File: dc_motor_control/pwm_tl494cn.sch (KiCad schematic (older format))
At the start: 31 parts

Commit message: New PCB for DC motor control
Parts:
- removed U?: L7812, symbol L7812
- added C1: 2200uF, Capacitors_ThroughHole:CP_Radial_D12.5mm_P5.00mm, symbol CP
- added C6: 1uF, Capacitors_ThroughHole:C_Rect_L4.6mm_W2.0mm_P2.50mm_MKS02_FKP02, symbol C
- added C7: 100nF, Capacitors_ThroughHole:C_Rect_L4.6mm_W2.0mm_P2.50mm_MKS02_FKP02, symbol C
- added D1: 15V, Diodes_ThroughHole:D_T-1_P5.08mm_Horizontal, symbol D_Zener
- added D6: LED, LEDs:LED_D4.0mm, symbol LED
- added J2: 12V_SEL, Pin_Headers:Pin_Header_Straight_1x03_Pitch2.54mm, symbol Conn_01x03
- added Q1: RFP70N06, TO_SOT_Packages_THT:TO-220-3_Vertical, symbol IRF540N
- added R1: 10R, Capacitors_ThroughHole:C_Rect_L4.6mm_W2.0mm_P2.50mm_MKS02_FKP02, symbol R
- added R13: 330R, Capacitors_ThroughHole:C_Rect_L4.6mm_W2.0mm_P2.50mm_MKS02_FKP02, symbol R
- added R14: 2K7, Capacitors_ThroughHole:C_Rect_L4.6mm_W2.0mm_P2.50mm_MKS02_FKP02, symbol R
- added R6: 1K, Capacitors_ThroughHole:C_Rect_L4.6mm_W2.0mm_P2.50mm_MKS02_FKP02, symbol R
- added U1: LM317, TO_SOT_Packages_SMD:SOT-223-3_TabPin2, symbol LM317_3PinPackage
- C2: renamed from C?; value 100uF -> 10uF; footprint (none) -> Capacitors_ThroughHole:CP_Radial_D4.0mm_P2.00mm
- C3, C4, C5: renamed from C?; footprint Capacitors_ThroughHole:C_Rect_L4_W2.5_P2.5 -> Capacitors_ThroughHole:C_Rect_L4.6mm_W2.0mm_P2.50mm_MKS02_FKP02
- D2, D3, D4, D5: renamed from D?; footprint (none) -> Diodes_ThroughHole:D_T-1_P5.08mm_Horizontal
- D7, D8: renamed from D?; footprint (none) -> TO_SOT_Packages_THT:TO-220-2_Vertical
- F1: renamed from F?; footprint (none) -> Fuse_Holders_and_Fuses:Fuse_SMD1206_Wave
- J1, J3: renamed from J?; footprint (none) -> Terminal_Blocks:TerminalBlock_Altech_AK300-2_P5.00mm
- Q2, Q3, Q4: renamed from Q?; footprint TO_SOT_Packages_THT:TO-220_Vertical -> TO_SOT_Packages_THT:TO-220-3_Vertical
- R10, R11, R12, R2, R3, R4, R5, R7, R8, R9: renamed from R?; footprint Resistors_Universal:Resistor_SMD+THTuniversal_2512_RM10_HandSoldering -> Capacitors_ThroughHole:C_Rect_L4.6mm_W2.0mm_P2.50mm_MKS02_FKP02
- RV1: renamed from RV?; value POT -> 5K; footprint (none) -> Potentiometers:Potentiometer_Piher_T16H_Single_Vertical
- U2: renamed from U?; footprint (none) -> SMD_Packages:SO-16-N
- gave numbers to parts that had none: 2
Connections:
- net +12V: now also R6.2
- net GND: now also RV1.3, C1.2, C6.2, C7.2, D1.2 (A), D6.1 (K), Q1.3 (S), R14.2; no longer RV1.1
- net at C5.2, R12.1, U2.14 (Vref): now also RV1.1; no longer RV1.3
- net at R5.2: now also J2.2 (Pin_2)
- net at D7.1 (K), D8.1 (K), F1.2: now also J3.1 (Pin_1), C1.1, C7.1, J2.3 (Pin_3), U1.3 (VI); no longer J3.2 (Pin_2)
- net at D7.2 (A), D8.2 (A), Q2.2 (D)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: now also J3.2 (Pin_2), Q1.2 (D); no longer J3.1 (Pin_1)
- net at D5.2 (A), R2.1, R3.1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: now also R1.1
- new net: D6.2 (A), R6.1
- new net: C6.1, J2.1 (Pin_1), R13.1, U1.2 (VO)
- new net: D1.1 (K), Q1.1 (G), R1.2
- new net: R13.2, R14.1, U1.1 (ADJ)
- no-connect marks 0 -> 1
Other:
- moved on the sheet: C2, C3, C4, C5, D2, D3, D4, D5, D7, D8, F1, J1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

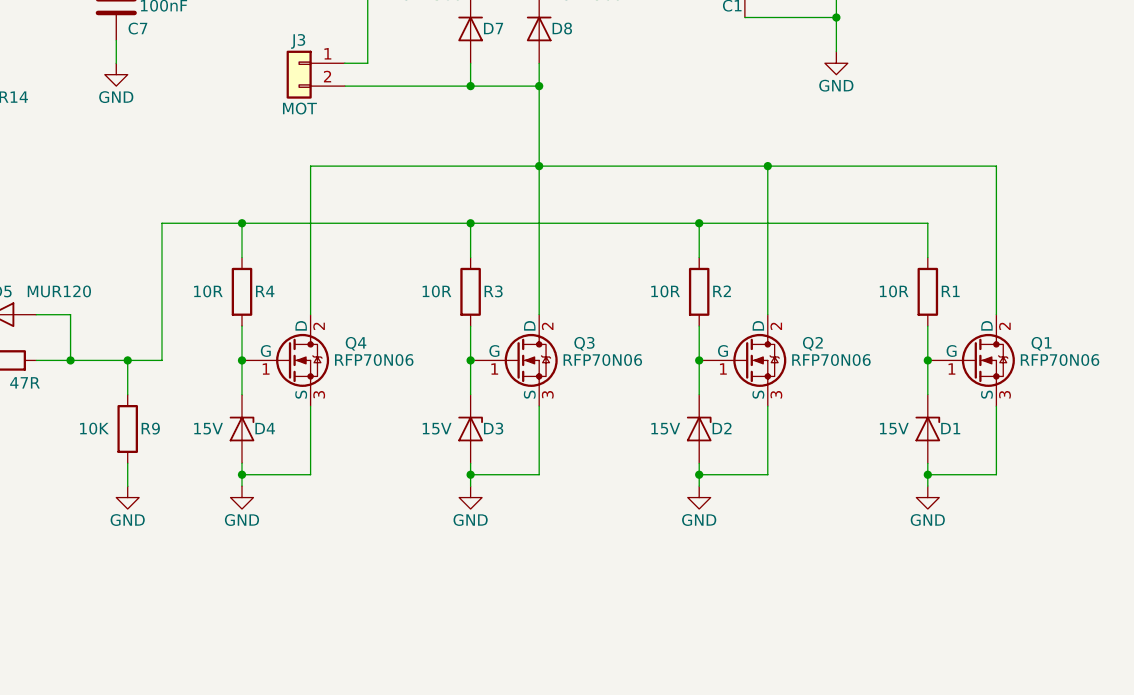
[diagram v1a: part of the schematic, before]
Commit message: Refining the DC motor control some more
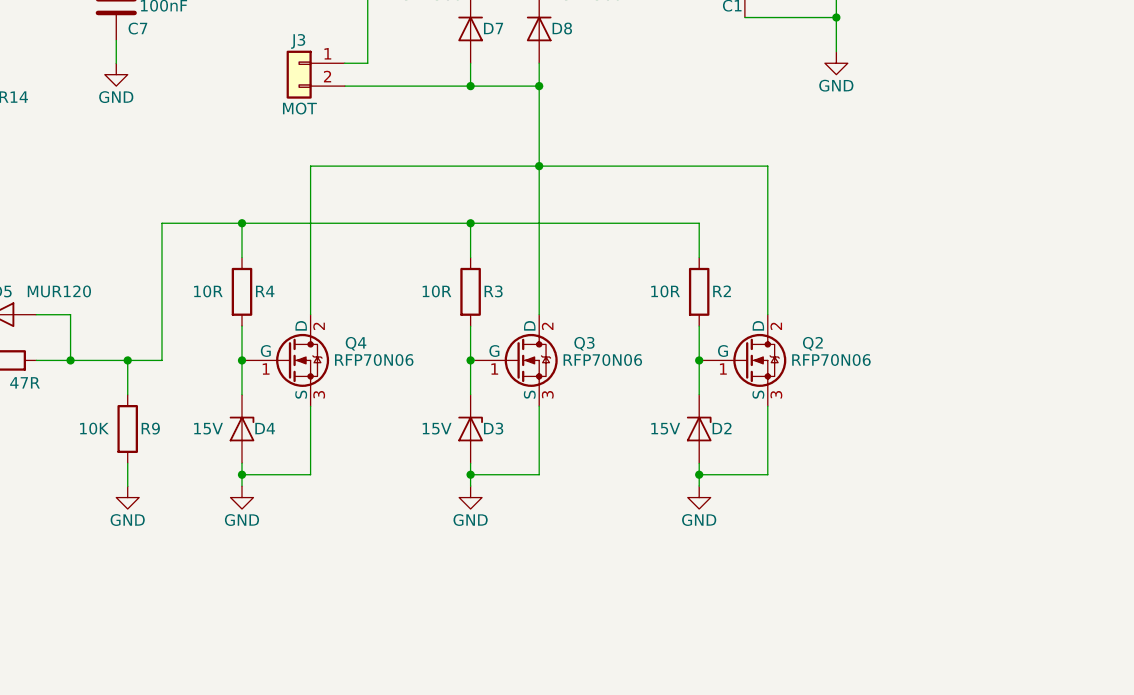
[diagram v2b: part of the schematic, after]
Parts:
- removed D1: 15V, Diodes_ThroughHole:D_T-1_P5.08mm_Horizontal, symbol D_Zener
- removed Q1: RFP70N06, TO_SOT_Packages_THT:TO-220-3_Vertical, symbol IRF540N
- removed R1: 10R, Capacitors_ThroughHole:C_Rect_L4.6mm_W2.0mm_P2.50mm_MKS02_FKP02, symbol R
- J1, J3: footprint Terminal_Blocks:TerminalBlock_Altech_AK300-2_P5.00mm -> Terminal_Blocks:TerminalBlock_bornier-2_P5.08mm
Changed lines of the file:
@@
 F 0 "J1" H 9900 2550 50  0000 C CNN
 F 1 "PWR" H 9900 2250 50  0000 C CNN
-F 2 "Terminal_Blocks:TerminalBlock_Altech_AK300-2_P5.00mm" H 9900 2450 50  0001 C CNN
+F 2 "Terminal_Blocks:TerminalBlock_bornier-2_P5.08mm" H 9900 2450 50  0001 C CNN
 F 3 "" H 9900 2450 50  0001 C CNN
 	1    9900 2450
@@
 F 0 "J3" H 6800 3050 50  0000 C CNN
 F 1 "MOT" H 6800 2750 50  0000 C CNN
-F 2 "Terminal_Blocks:TerminalBlock_Altech_AK300-2_P5.00mm" H 6800 2950 50  0001 C CNN
+F 2 "Terminal_Blocks:TerminalBlock_bornier-2_P5.08mm" H 6800 2950 50  0001 C CNN
 F 3 "" H 6800 2950 50  0001 C CNN
 	1    6800 2950
@@
 $EndComp
 $Comp
-L IRF540N Q1
-U 1 1 5B9B1991
-P 9750 4250
-F 0 "Q1" H 10000 4325 50  0000 L CNN
-F 1 "RFP70N06" H 9950 4250 50  0000 L CNN
-F 2 "TO_SOT_Packages_THT:TO-220-3_Vertical" H 10000 4175 50  0001 L CIN
-F 3 "" H 9750 4250 50  0001 L CNN
-	1    9750 4250
-	1    0    0    -1
-$EndComp
-$Comp
-L R R1
-U 1 1 5B9B1A3F
-P 9550 3950
-F 0 "R1" H 9650 3950 50  0000 C CNN
-F 1 "10R" H 9400 3950 50  0000 C CNN
-F 2 "Capacitors_ThroughHole:C_Rect_L4.6mm_W2.0mm_P2.50mm_MKS02_FKP02" V 9480 3950 50  0001 C CNN
-F 3 "" H 9550 3950 50  0000 C CNN
-	1    9550 3950
-	1    0    0    -1
-$EndComp
-$Comp
-L D_Zener D1
-U 1 1 5B9B1AE4
-P 9550 4550
-F 0 "D1" V 9550 4650 50  0000 C CNN
-F 1 "15V" V 9550 4400 50  0000 C CNN
-F 2 "Diodes_ThroughHole:D_T-1_P5.08mm_Horizontal" H 9550 4550 50  0001 C CNN
-F 3 "" H 9550 4550 50  0001 C CNN
-	1    9550 4550
-	0    1    1    0
-$EndComp
-$Comp
-L GND #PWR015
-U 1 1 5B9B1B8A
-P 9550 4800
-F 0 "#PWR015" H 9550 4550 50  0001 C CNN
-F 1 "GND" H 9550 4650 50  0000 C CNN
-F 2 "" H 9550 4800 50  0000 C CNN
-F 3 "" H 9550 4800 50  0000 C CNN
-	1    9550 4800
-	1    0    0    -1
-$EndComp
-$Comp
-L +12V #PWR016
+L +12V #PWR015
 U 1 1 5B9BEB96
 P 2950 1650
-F 0 "#PWR016" H 2950 1500 50  0001 C CNN
+F 0 "#PWR015" H 2950 1500 50  0001 C CNN
 F 1 "+12V" H 2950 1790 50  0000 C CNN
 F 2 "" H 2950 1650 50  0001 C CNN
@@
 $EndComp
 $Comp
-L GND #PWR017
+L GND #PWR016
 U 1 1 5B9BEC13
 P 2950 2250
-F 0 "#PWR017" H 2950 2000 50  0001 C CNN
+F 0 "#PWR016" H 2950 2000 50  0001 C CNN
 F 1 "GND" H 2950 2100 50  0000 C CNN
 F 2 "" H 2950 2250 50  0000 C CNN
@@
 Wire Wire Line
 	5700 2450 9200 2450
-Connection ~ 8850 3400
-Wire Wire Line
-	9850 3400 9850 4050
-Connection ~ 8550 3650
-Wire Wire Line
-	9550 3650 9550 3800
-Connection ~ 9550 4750
-Wire Wire Line
-	9850 4750 9850 4450
-Wire Wire Line
-	9550 4750 9850 4750
-Wire Wire Line
-	9550 4700 9550 4800
-Connection ~ 9550 4250
-Wire Wire Line
-	9550 4100 9550 4400
 Wire Wire Line
 	2400 1750 2550 1750
@@
 	7850 2950 7850 4050
 Wire Wire Line
-	6850 3400 9850 3400
+	6850 3400 8850 3400
 Wire Wire Line
 	6850 4050 6850 3400
@@
 	6550 3650 6550 3800
 Wire Wire Line
-	6200 3650 9550 3650
+	6200 3650 8550 3650
 Wire Wire Line
 	6200 4250 6200 3650
@@
 Connection ~ 6000 2450
 $Comp
-L GND #PWR018
+L GND #PWR017
 U 1 1 5B9C206A
 P 6000 2950
-F 0 "#PWR018" H 6000 2700 50  0001 C CNN
+F 0 "#PWR017" H 6000 2700 50  0001 C CNN
 F 1 "GND" H 6000 2800 50  0000 C CNN
 F 2 "" H 6000 2950 50  0000 C CNN
@@
 $EndComp
 $Comp
-L GND #PWR019
+L GND #PWR018
 U 1 1 5B9C3BD8
 P 4050 2950
-F 0 "#PWR019" H 4050 2700 50  0001 C CNN
+F 0 "#PWR018" H 4050 2700 50  0001 C CNN
 F 1 "GND" H 4050 2800 50  0000 C CNN
 F 2 "" H 4050 2950 50  0000 C CNN
@@
 $EndComp
 $Comp
-L GND #PWR020
+L GND #PWR019
 U 1 1 5B9C420E
 P 5400 3350
-F 0 "#PWR020" H 5400 3100 50  0001 C CNN
+F 0 "#PWR019" H 5400 3100 50  0001 C CNN
 F 1 "GND" H 5400 3200 50  0000 C CNN
 F 2 "" H 5400 3350 50  0000 C CNN
